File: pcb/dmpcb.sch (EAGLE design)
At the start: 44 parts, among them IC1 7805DT, IC2 L293D, IC3 MAX7219CNG, Q1 IRF530, Q2 IRF530

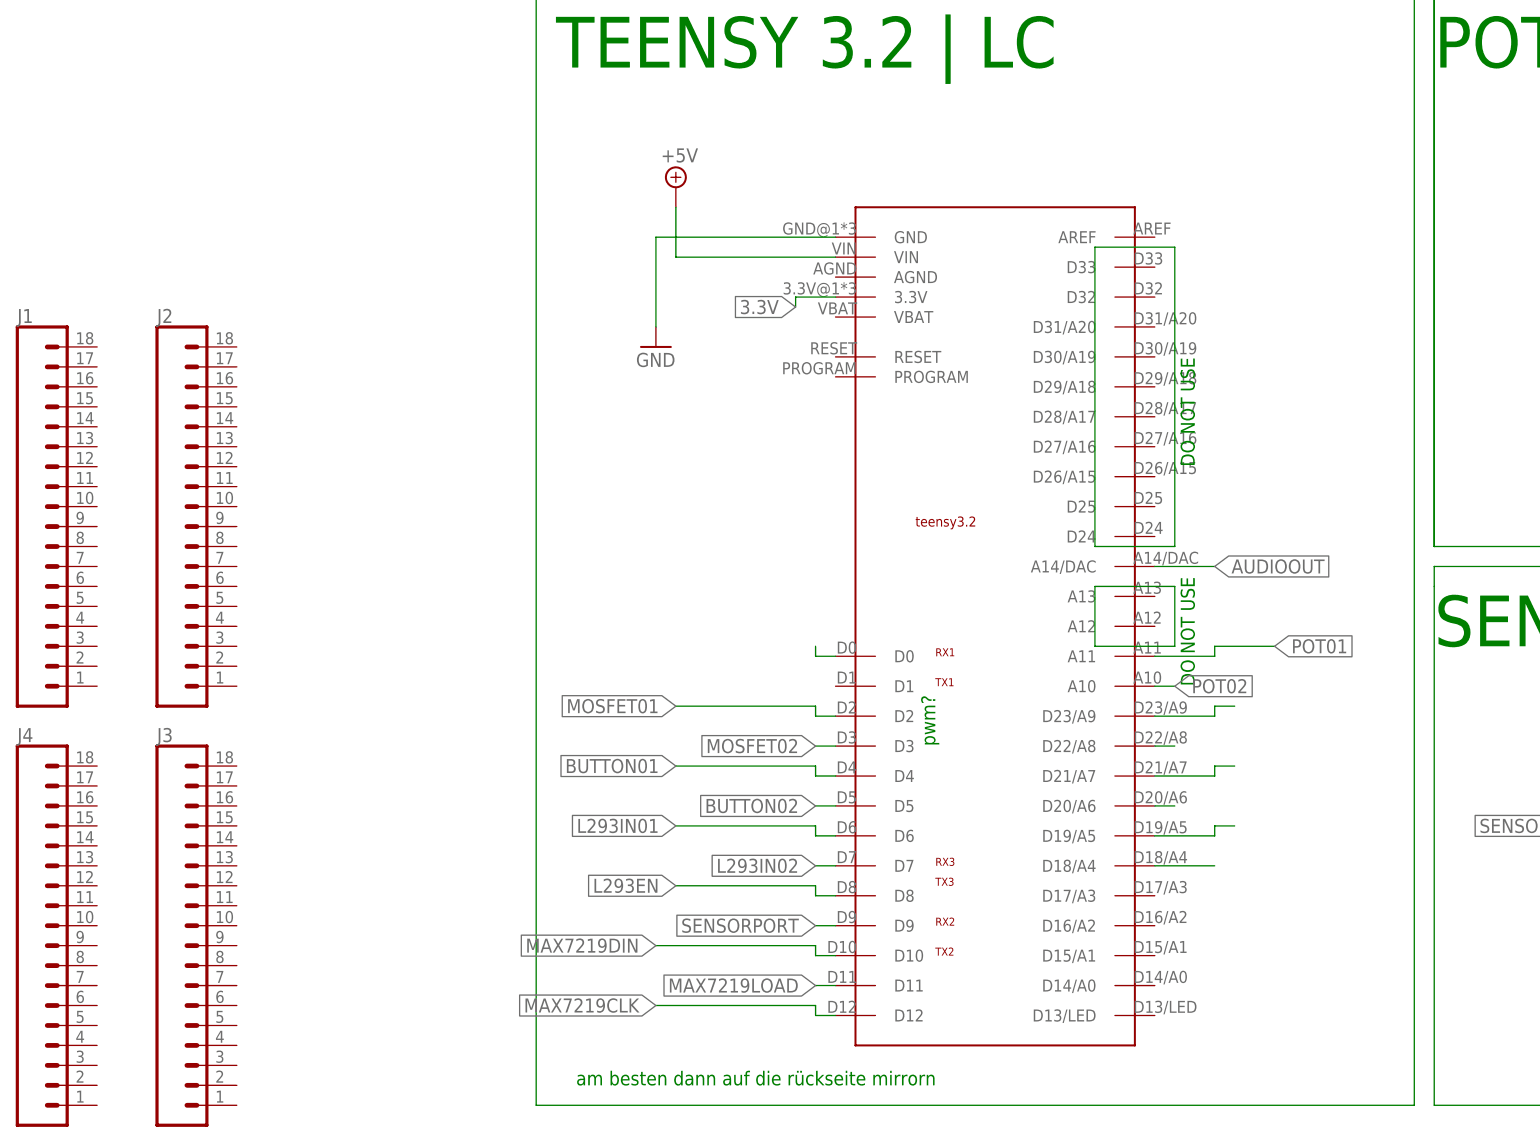
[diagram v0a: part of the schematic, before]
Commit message: added other teensy lib, has better pin spacing, also added breakout jumpers for all pins (-RX and TX)
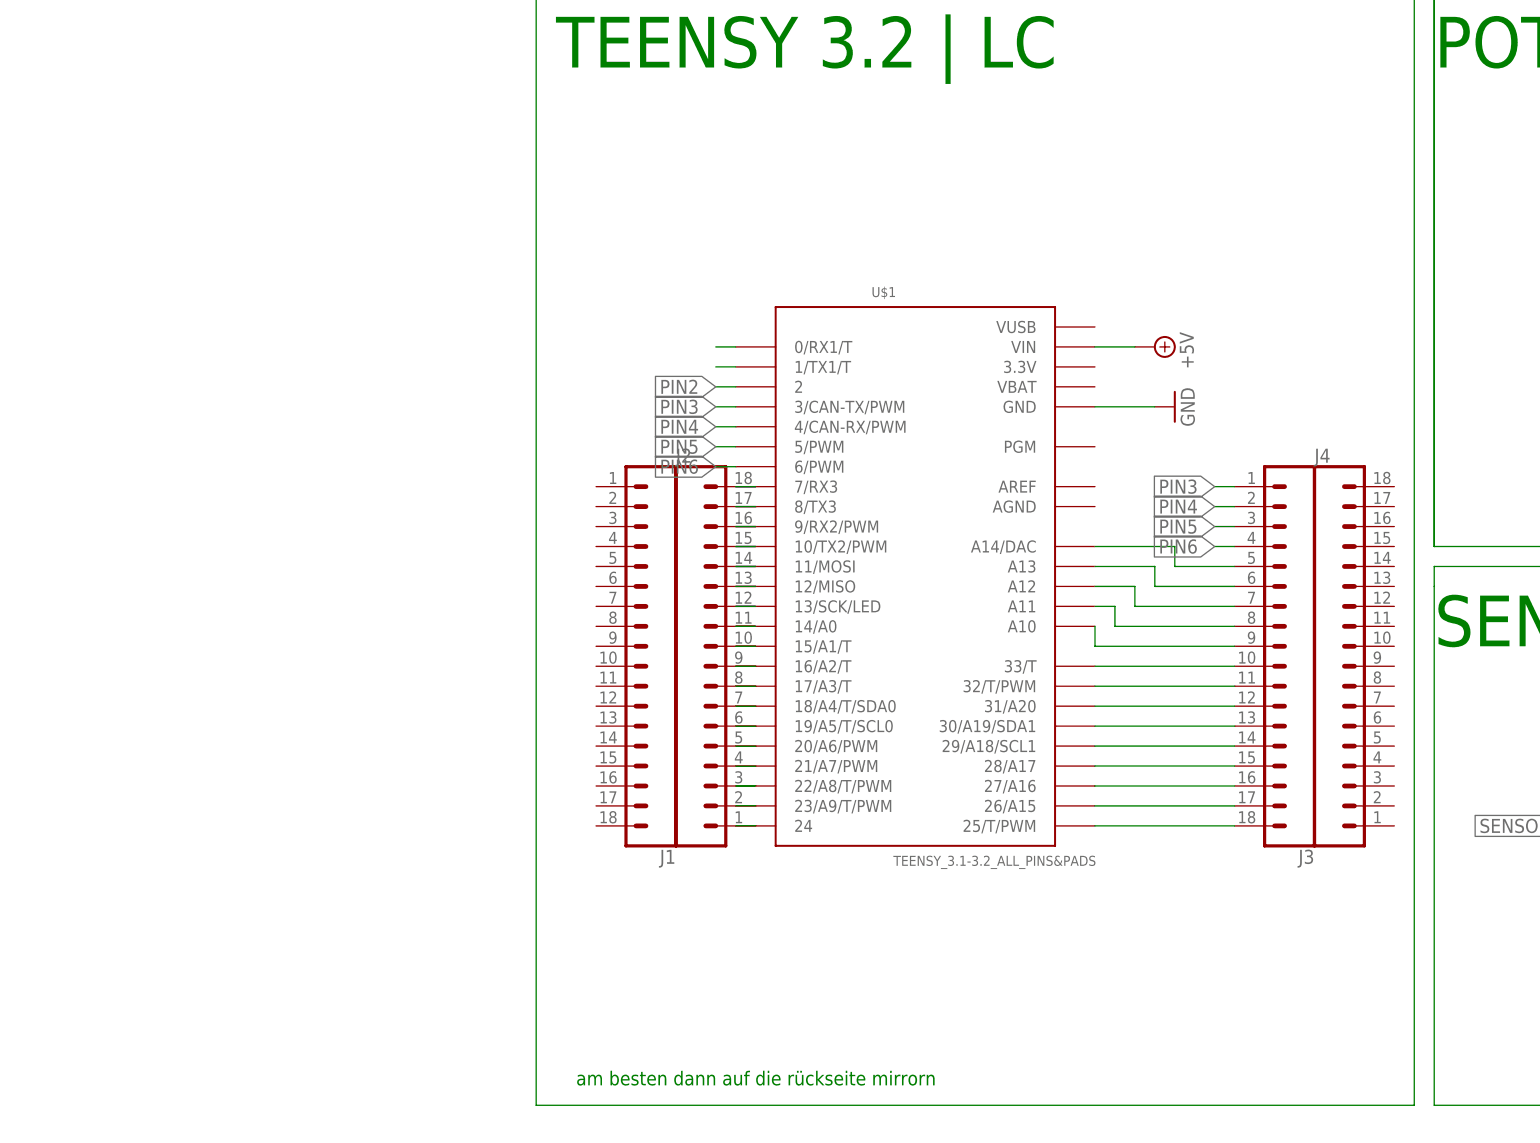
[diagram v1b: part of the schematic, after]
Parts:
- U$1: value TEENSY3.1_ALL -> TEENSY_3.1-3.2_ALL_PINS&PADS; device Teensy3.1_ralfsfix:TEENSY3.1_ALL -> Teensy_3_and_LC_Series_Boards_v1.4:TEENSY_3.1-3.2_ALL_PINS&PADS
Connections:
- removed net AUDIOOUT: U$1.A14/DAC
- removed net POT1: U$1.D22/A8
- removed net POT2: U$1.D18/A4
- new net N$22: J2.1, U$1.24
- new net N$23: J2.2, U$1.23/A9/T/PWM
- new net N$26: J2.3, U$1.22/A8/T/PWM
- new net N$27: J2.4, U$1.21/A7/PWM
- new net N$28: J2.5, U$1.20/A6/PWM
- new net N$30: J2.7, U$1.18/A4/T/SDA0
- new net N$31: J2.8, U$1.17/A3/T
- new net N$36: J2.13, U$1.12/MISO
- new net N$37: J2.14, U$1.11/MOSI
- new net N$38: J2.15, U$1.10/TX2/PWM
- new net N$39: J2.16, U$1.9/RX2/PWM
- new net N$40: J2.17, U$1.8/TX3
- new net N$41: J2.18, U$1.7/RX3
- new net N$42: J3.18, U$1.25/T/PWM
- new net N$43: J3.17, U$1.26/A15
- new net N$44: J3.16, U$1.27/A16
- new net N$45: J3.15, U$1.28/A17
- new net N$46: J3.14, U$1.29/A18/SCL1
- new net N$47: J3.13, U$1.30/A19/SDA1
- new net N$48: J3.12, U$1.31/A20
- new net N$49: J3.11, U$1.32/T/PWM
- new net N$50: J3.10, U$1.33/T
- new net N$51: J3.9, U$1.A10
- new net N$52: J3.8, U$1.A11
- new net N$53: J3.7, U$1.A12
- new net N$54: J3.6, U$1.A13
- new net N$55: J3.5, U$1.A14/DAC
- new net N$61: U$1.1/TX1/T
- new net N$62: U$1.0/RX1/T
- new net PIN2: U$1.2
- new net PIN3: J3.1, U$1.3/CAN-TX/PWM
- new net PIN4: J3.2, U$1.4/CAN-RX/PWM
- new net PIN5: J3.3, U$1.5/PWM
- new net PIN6: J3.4, U$1.6/PWM
- net 3.3V: no longer U$1.3.3V
- net BUTTON01: no longer U$1.D4
- net BUTTON02: no longer U$1.D5
- net L293EN: no longer U$1.D8
- net L293IN01: no longer U$1.D6
- net L293IN02: no longer U$1.D7
- net MAX7219CLK: no longer U$1.D12
- net MAX7219DIN: no longer U$1.D10
- net MAX7219LOAD: no longer U$1.D11
- net MOSFET01: no longer U$1.D2
- net MOSFET02: no longer U$1.D3
- net N$29: now also J2.6, U$1.19/A5/T/SCL0; no longer U$1.D0
- net N$32: now also J2.9, U$1.16/A2/T; no longer U$1.D23/A9
- net N$33: now also J2.10, U$1.15/A1/T; no longer U$1.D21/A7
- net N$34: now also J2.11, U$1.14/A0; no longer U$1.D19/A5
- net N$35: now also J2.12, U$1.13/SCK/LED; no longer U$1.D20/A6
- net POT01: no longer U$1.A11
- net POT02: no longer U$1.A10
- net SENSORPORT: no longer U$1.D9
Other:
- note removed: "DO NOT USE"
- note removed: "pwm?"
- moved on the sheet: J1, J2, J3, J4

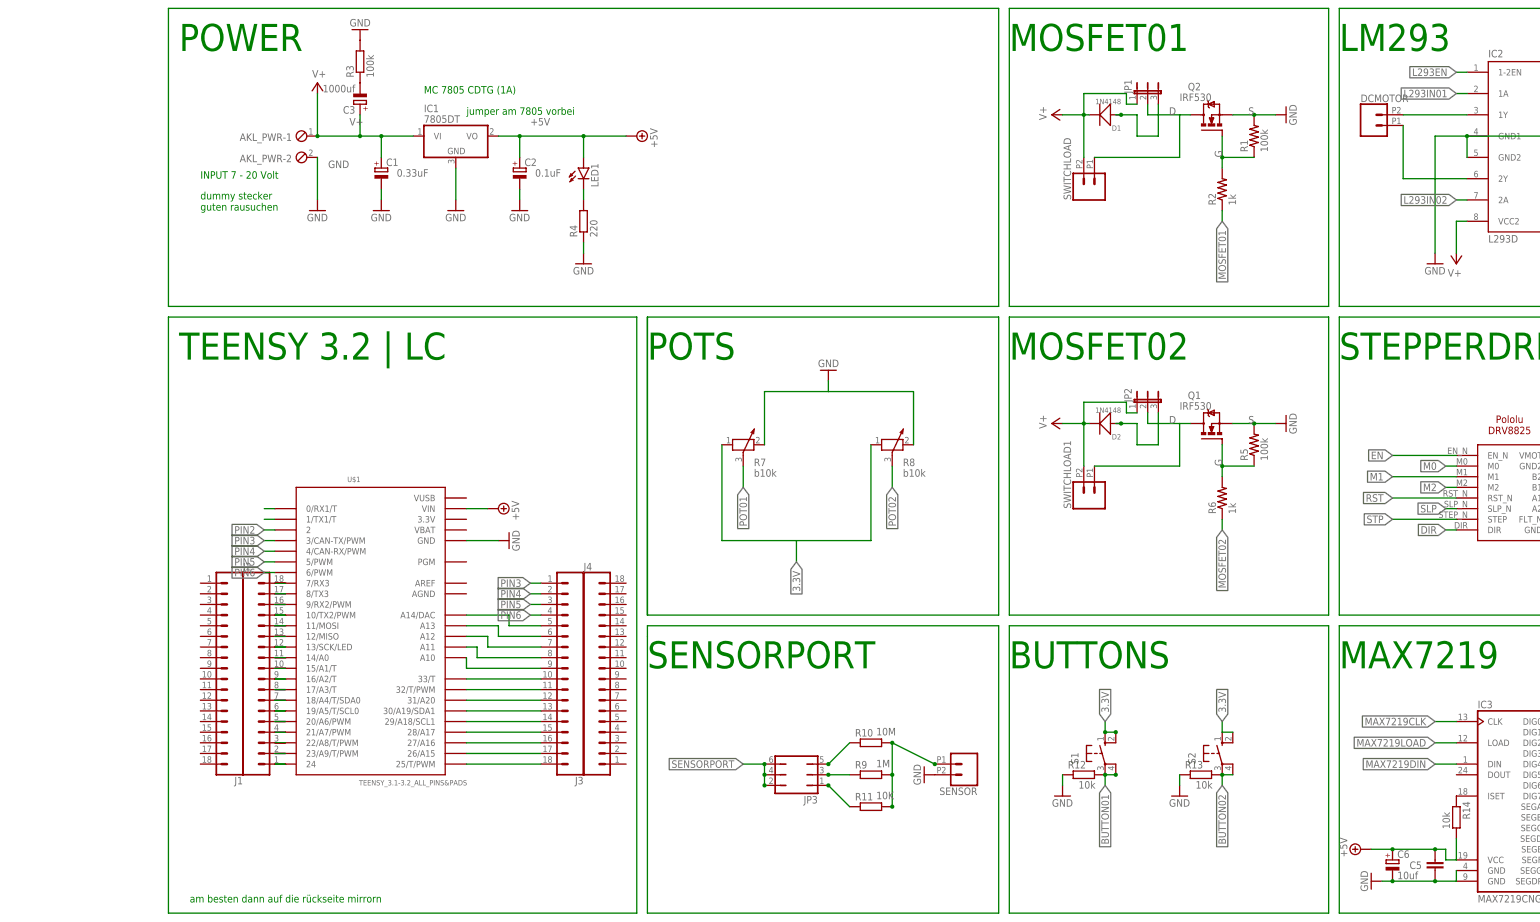
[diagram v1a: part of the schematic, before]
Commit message: fixed drv8825, also added lm358
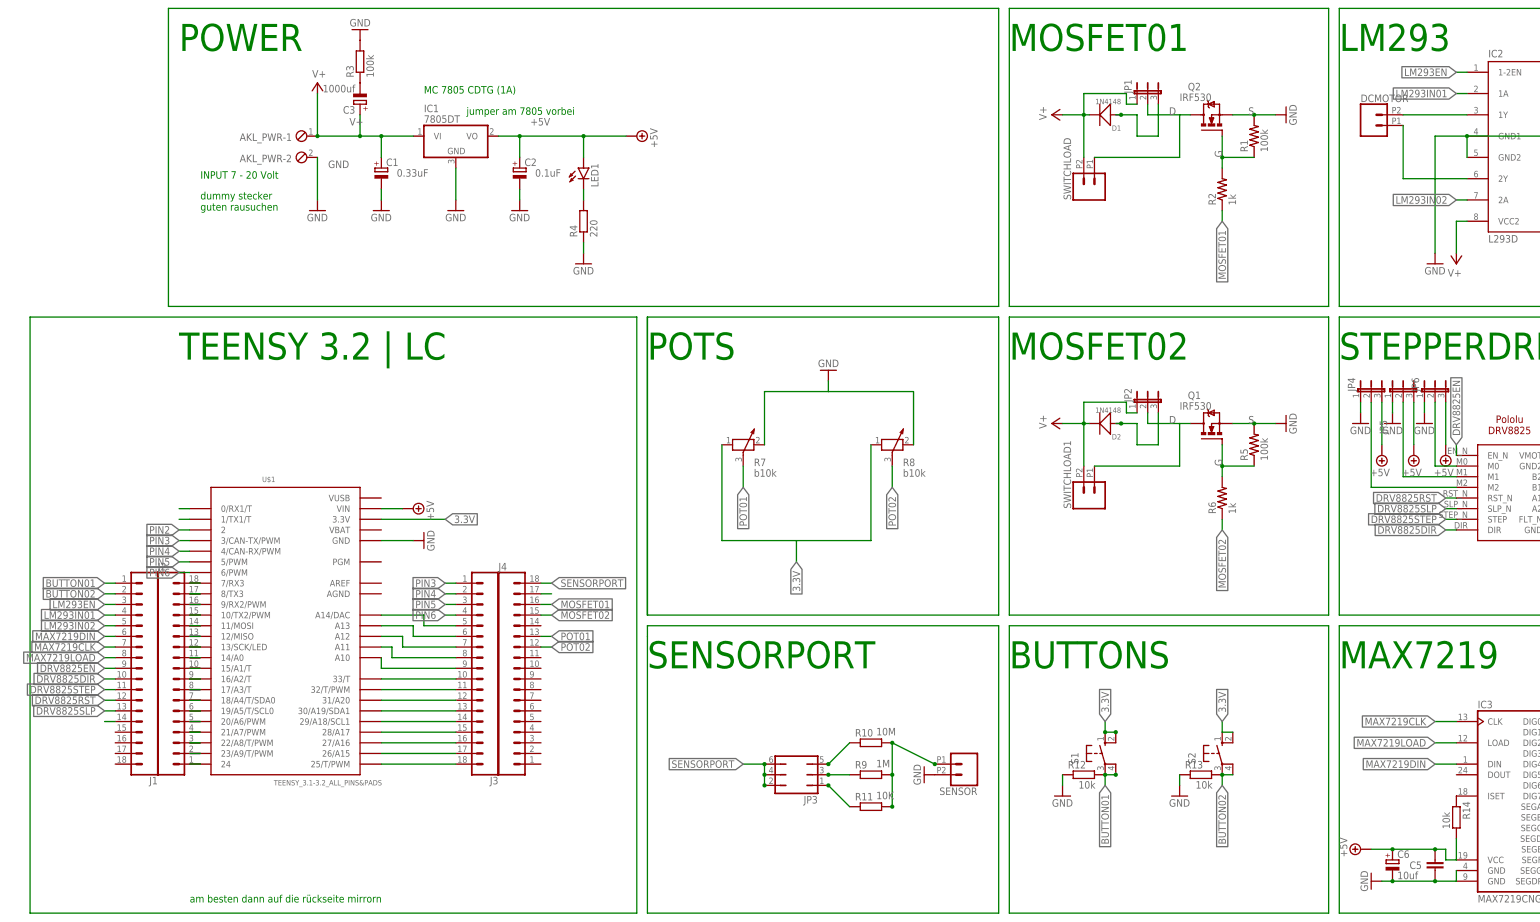
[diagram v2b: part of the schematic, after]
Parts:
- added JP4, JP5, JP6: (no value), jumper:JP2E
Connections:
- removed net DIR: U$2.DIR
- removed net EN: U$2.EN_N
- removed net L293EN: IC2.1-2EN
- removed net L293IN01: IC2.1A
- removed net L293IN02: IC2.2A
- removed net M0: U$2.M0
- removed net M1: U$2.M1
- removed net M2: U$2.M2
- removed net RST: U$2.RST_N
- removed net SLP: U$2.SLP_N
- removed net STP: U$2.STEP
- new net DRV8825DIR: J1.10, U$2.DIR
- new net DRV8825EN: J1.9, U$2.EN_N
- new net DRV8825RST: J1.12, U$2.RST_N
- new net DRV8825SLP: J1.13, U$2.SLP_N
- new net DRV8825STEP: J1.11, U$2.STEP
- new net LM293EN: IC2.1-2EN, J1.3
- new net LM293IN01: IC2.1A, J1.4
- new net LM293IN02: IC2.2A, J1.5
- new net N$56: J4.17
- new net N$57: JP4.2, U$2.M2
- new net N$58: JP5.2, U$2.M1
- new net N$59: JP6.2, U$2.M0
- new net N$64: J1.14
- net +5V: now also JP4.3, JP5.3, JP6.3
- net 3.3V: now also U$1.3.3V
- net BUTTON01: now also J1.1
- net BUTTON02: now also J1.2
- net GND: now also JP4.1, JP5.1, JP6.1
- net MAX7219CLK: now also J1.7
- net MAX7219DIN: now also J1.6
- net MAX7219LOAD: now also J1.8
- net MOSFET01: now also J4.16
- net MOSFET02: now also J4.15
- net POT01: now also J4.13
- net POT02: now also J4.12
- net SENSORPORT: now also J4.18
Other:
- moved on the sheet: J1, J2, J3, J4, U$1

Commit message: need to add custom component for dotmatrix display
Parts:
- added IC4: LM358D, linear:LM358D
- added R15, R16: 10K, rcl:R-EU_M0805
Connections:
- new net N$65: IC4A.-IN, R15.2, R16.1
- new net OPAMPIN: IC4A.+IN
- new net OPAMPOUT: IC4A.OUT, J4.10, R15.1
- net +5V: now also IC4P.V+
- net GND: now also IC4P.V-, R16.2
- net SENSORPORT: now also J4.11
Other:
- note added: "OPAMP"
- note removed: "TODO Sensorport mit variablem pull up/pull down mit jumper oder schiebeschalter mit trimmer und kleinem widerstand -> Done Dotmatrix mit max7219 Anschlüsse gejumpert, wenn was anderes angesclossen werden soll, jumper ziehen Potis b10k -> done Buttons -> done Farbcode für jumper LM293 Strom von 12v in -> done Opamp-Verstärker"
- note removed: "am besten dann auf die rückseite mirrorn"
- moved on the sheet: AKL_PWR-1, AKL_PWR-2, C1, C2, C3, IC1, JP3, LED1, R10, R11, R3, R4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

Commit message: added jumper around 7805, if 5v load is bigger than 1Amp
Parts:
- added JP7: (no value), jumper:JP1E
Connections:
- net +5V: now also JP7.2
- net V+: now also JP7.1
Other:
- note removed: "jumper am 7805 vorbei"
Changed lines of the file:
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@@
 <part name="R16" library="rcl" library_urn="urn:adsk.eagle:library:334" deviceset="R-EU_" device="M0805" package3d_urn="urn:adsk.eagle:package:23556/1" value="10K"/>
 <part name="GND23" library="supply1" library_urn="urn:adsk.eagle:library:371" deviceset="GND" device=""/>
+<part name="JP7" library="jumper" library_urn="urn:adsk.eagle:library:252" deviceset="JP1E" device="" package3d_urn="urn:adsk.eagle:package:15455/1"/>
 </parts>
 <sheets>
@@
 <text x="152.4" y="203.2" size="6.4516" layer="91">POTS</text>
 <text x="317.5" y="129.54" size="6.4516" layer="91">STEPPERDRIVER</text>
-<text x="76.2" y="187.96" size="1.778" layer="91">jumper am 7805 vorbei</text>
 <text x="152.4" y="129.54" size="6.4516" layer="91">SENSORPORT</text>
 <text x="238.76" y="55.88" size="6.4516" layer="91">BUTTONS</text>
@@
 <instance part="GND23" gate="1" x="208.28" y="5.08" smashed="yes">
 <attribute name="VALUE" x="205.74" y="2.54" size="1.778" layer="96"/>
+</instance>
+<instance part="JP7" gate="A" x="68.58" y="200.66" smashed="yes">
+<attribute name="NAME" x="67.31" y="200.66" size="1.778" layer="95" rot="R90"/>
+<attribute name="VALUE" x="74.295" y="200.66" size="1.778" layer="96" rot="R90"/>
 </instance>
 </instances>
@@
 <junction x="40.64" y="182.88"/>
 <pinref part="C1" gate="G$1" pin="+"/>
-<wire x1="50.8" y1="182.88" x2="55.88" y2="182.88" width="0.1524" layer="91"/>
+<wire x1="50.8" y1="182.88" x2="53.34" y2="182.88" width="0.1524" layer="91"/>
+<wire x1="53.34" y1="182.88" x2="55.88" y2="182.88" width="0.1524" layer="91"/>
 <wire x1="55.88" y1="182.88" x2="63.5" y2="182.88" width="0.1524" layer="91"/>
 <wire x1="55.88" y1="182.88" x2="55.88" y2="177.8" width="0.1524" layer="91"/>
@@
 <wire x1="50.8" y1="187.96" x2="50.8" y2="182.88" width="0.1524" layer="91"/>
 <junction x="50.8" y="182.88"/>
+<pinref part="JP7" gate="A" pin="1"/>
+<wire x1="53.34" y1="198.12" x2="68.58" y2="198.12" width="0.1524" layer="91"/>
+<wire x1="53.34" y1="198.12" x2="53.34" y2="182.88" width="0.1524" layer="91"/>
+<junction x="53.34" y="182.88"/>
 </segment>
 <segment>
@@
 <segment>
 <pinref part="IC1" gate="A1" pin="VO"/>
-<wire x1="83.82" y1="182.88" x2="88.9" y2="182.88" width="0.1524" layer="91"/>
 <label x="91.44" y="185.42" size="1.778" layer="95"/>
 <pinref part="SUPPLY2" gate="+5V" pin="+5V"/>
 <pinref part="C2" gate="G$1" pin="+"/>
-<wire x1="88.9" y1="182.88" x2="104.14" y2="182.88" width="0.1524" layer="91"/>
+<wire x1="83.82" y1="182.88" x2="88.9" y2="182.88" width="0.1524" layer="91"/>
+<wire x1="88.9" y1="182.88" x2="93.98" y2="182.88" width="0.1524" layer="91"/>
+<wire x1="93.98" y1="182.88" x2="104.14" y2="182.88" width="0.1524" layer="91"/>
 <wire x1="104.14" y1="182.88" x2="114.3" y2="182.88" width="0.1524" layer="91"/>
 <wire x1="88.9" y1="182.88" x2="88.9" y2="177.8" width="0.1524" layer="91"/>
@@
 <wire x1="104.14" y1="177.8" x2="104.14" y2="182.88" width="0.1524" layer="91"/>
 <junction x="104.14" y="182.88"/>
-</segment>
-<segment>
+<pinref part="JP7" gate="A" pin="2"/>
+<wire x1="71.12" y1="198.12" x2="93.98" y2="198.12" width="0.1524" layer="91"/>
+<wire x1="93.98" y1="198.12" x2="93.98" y2="182.88" width="0.1524" layer="91"/>
+<junction x="93.98" y="182.88"/>
+</segment>
+<segment>

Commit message: added felix' better audio output (thank you felix). still need to find use for one half opamp. Ideas?
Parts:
- added C4: 100nf, rcl:C-EUC0805
- added C8, C9: 100uf, rcl:CPOL-EUB
- added IC5: LM358D, linear:LM358D
- added J5, J6: (no value), SparkFun-Connectors:CONN_05
- added J7: SJ-3523-SMT-TR, SJ-3523-SMT-TR:SJ-3523-SMT-TR
- added R17, R19: b10k, pot:TRIM_EU-RJ9W
- added R18: 270R, rcl:R-EU_M0805
- added R20: 10K, rcl:R-EU_M0805
- added R21: b100k, pot:TRIM_EU-RJ9W
- R15: value 10K -> b100k; device rcl:R-EU_M0805 -> pot:TRIM_EU-RJ9W
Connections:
- removed net N$65: IC4A.-IN, R15.2, R16.1
- new net BETTERAUDIOOUT: J4.14, R17.E
- new net N$63: IC4A.-IN, R15.A, R16.1
- new net N$66: C8.+, J7.2
- new net N$67: R17.A, R17.S, R18.2
- new net N$68: C4.1, IC5A.+IN, R18.1
- new net N$69: IC5A.-IN, IC5A.OUT, R19.E
- new net N$71: IC5B.+IN, R19.S
- new net N$72: C8.-, C9.-, IC5B.-IN, IC5B.OUT
- new net N$73: C9.+, J7.3
- new net N$75: IC4B.-IN, R20.1, R21.A
- net +5V: now also IC5P.V+, J5.5
- net GND: now also C4.2, IC5P.V-, J5.4, J6.1, J6.2, J6.3, J6.4, J6.5, J7.1, R19.A, R20.2
- net MAX7219CLK: now also J5.1
- net MAX7219DIN: now also J5.3
- net MAX7219LOAD: now also J5.2
- net OPAMPIN: now also IC4B.+IN
- net OPAMPOUT: now also IC4B.OUT, R15.E, R15.S, R21.E, R21.S; no longer R15.1
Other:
- note added: "BETTEROUT"
- note added: "designed by Felix Fisgus"
- moved on the sheet: C5, C6, IC3, R14, R16
